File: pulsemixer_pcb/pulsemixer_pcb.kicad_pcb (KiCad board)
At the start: 2 copper layers, 93 parts, among them SW101 SW_PG_RIGHT, SW102 SW_PG_LEFT, SW103 SW_STRM_DEV, SW201 Vol_Encoder, SW202 SW_MUTE, SW301 Vol_Encoder, SW302 SW_MUTE, SW401 Vol_Encoder, SW402 SW_MUTE, SW501 Vol_Encoder, SW502 SW_MUTE, U101 SN74LHC08DR, U102 SN74HC21DR, U201 MCP23017_SP, U202 74LVC2G14, U301 MCP23017_SP, U302 74LVC2G14, U401 MCP23017_SP, U402 74LVC2G14, U501 MCP23017_SP, U502 74LVC2G14

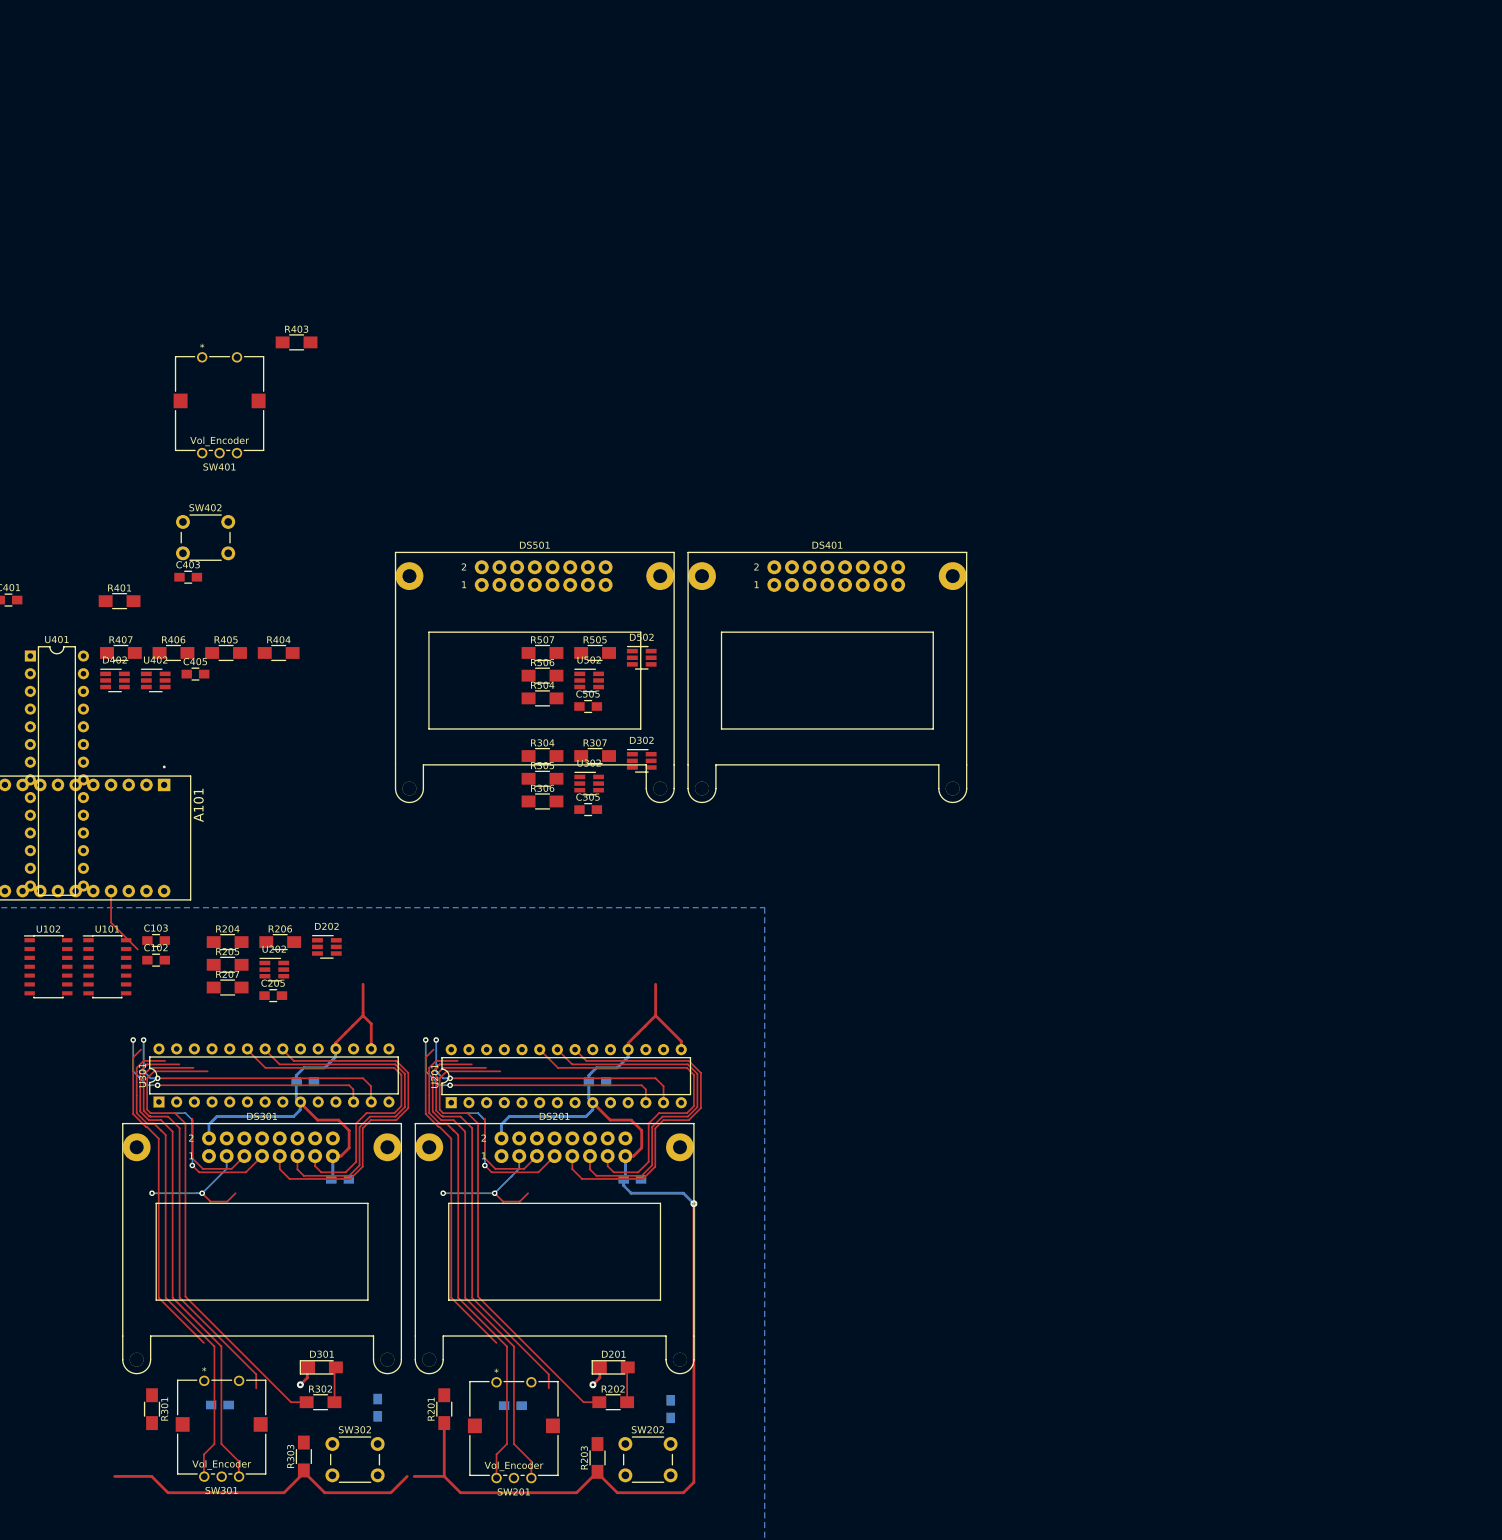
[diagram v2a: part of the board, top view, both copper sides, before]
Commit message: Rearranged LCD pins to allow for interrupts on both GPIO banks.
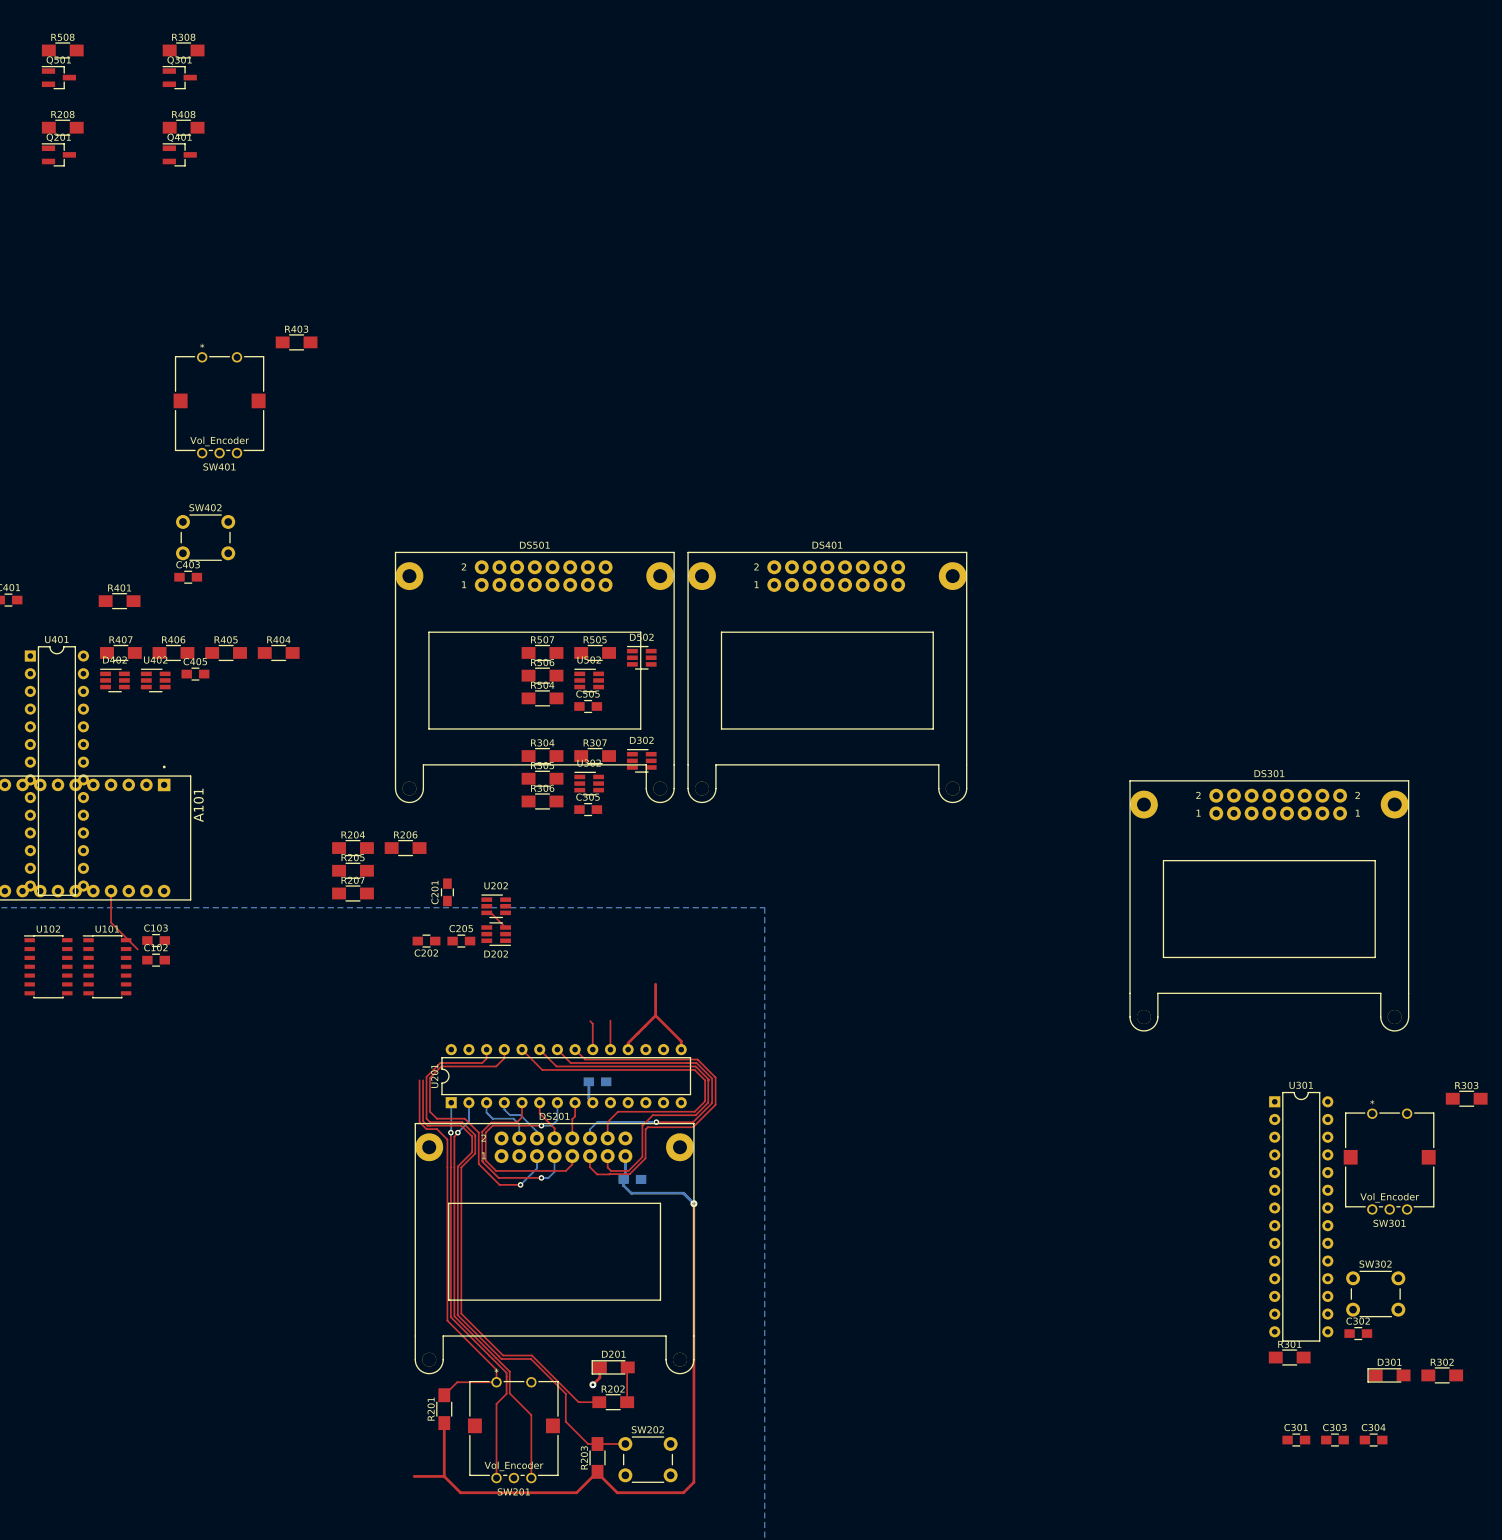
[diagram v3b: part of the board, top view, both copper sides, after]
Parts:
- added Q201: Q_NPN_CBE, TO_SOT_Packages_SMD:SOT-23_Handsoldering, F.Cu at (98.8, -86.1)
- added Q301: Q_NPN_CBE, TO_SOT_Packages_SMD:SOT-23_Handsoldering, F.Cu at (116.2, -97.2)
- added Q401: Q_NPN_CBE, TO_SOT_Packages_SMD:SOT-23_Handsoldering, F.Cu at (116.2, -86.1)
- added Q501: Q_NPN_CBE, TO_SOT_Packages_SMD:SOT-23_Handsoldering, F.Cu at (98.8, -97.2)
- added R208: 1K, Resistors_SMD:R_1206_HandSoldering, F.Cu at (99.4, -90.0)
- added R308: 1K, Resistors_SMD:R_1206_HandSoldering, F.Cu at (116.7, -101.1)
- added R408: 1K, Resistors_SMD:R_1206_HandSoldering, F.Cu at (116.7, -90.0)
- added R508: 1K, Resistors_SMD:R_1206_HandSoldering, F.Cu at (99.4, -101.1)
- C201, C202, C301, C302, C303, C304: moved to F.Cu
- moved R303 174.7 mm to (300.9, 49.4), turned to 0 degrees
- moved SW301 172.0 mm to (289.9, 72.4)
- moved C302 163.8 mm to (285.4, 83.2), turned to 0 degrees
- moved R301 163.5 mm to (275.5, 86.6), turned to 0 degrees
- moved R302 161.1 mm to (297.4, 89.2)
- moved U301 160.2 mm to (273.4, 49.9), turned to 0 degrees
- moved C303 156.5 mm to (282.0, 98.4)
- moved D301 153.3 mm to (289.9, 89.2)
- moved C304 153.0 mm to (287.6, 98.4)
- moved DS301 152.8 mm to (272.6, 3.80)
- moved SW302 148.5 mm to (284.6, 75.2)
- moved C301 132.0 mm to (276.5, 98.4), turned to 0 degrees
- moved C201 80.8 mm to (154.6, 19.8), turned to 90 degrees
- moved C202 67.8 mm to (151.6, 26.8)
- moved U202 33.1 mm to (161.6, 21.8)
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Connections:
- DS201 pad 16: GND -> Net-(DS201-Pad16)
- DS301 pad 16: GND -> Net-(DS301-Pad16)
- DS401 pad 16: GND -> Net-(DS401-Pad16)
- DS501 pad 16: GND -> Net-(DS501-Pad16)
- U201 pad 1: /Channel1/MUTE_SW -> /Channel1/VOL_A
- U201 pad 2: /Channel1/VOL_SW -> /Channel1/VOL_B
- U201 pad 21: /Channel1/LCD_DB2 -> /Channel1/LCD_DB4
- U201 pad 22: /Channel1/LCD_DB4 -> /Channel1/LCD_DB5
- U201 pad 24: /Channel1/LCD_DB5 -> /Channel1/LCD_DB7
- U201 pad 25: /Channel1/LCD_DB7 -> /Channel1/LCD_RW
- U201 pad 27: /Channel1/VOL_B -> /Channel1/MUTE_SW
- U201 pad 28: /Channel1/VOL_A -> /Channel1/VOL_SW
- U201 pad 3: /Channel1/LCD_DB0 -> /Channel1/LCD_RS
- U201 pad 4: /Channel1/LCD_RW -> /Channel1/LCD_E
- U201 pad 5: /Channel1/LCD_RS -> /Channel1/LCD_DB0
- U201 pad 6: /Channel1/LCD_E -> /Channel1/LCD_DB1
- U201 pad 7: /Channel1/LCD_DB1 -> /Channel1/LCD_DB2
- U301 pad 1: /Channel2/MUTE_SW -> /Channel2/VOL_A
- U301 pad 2: /Channel2/VOL_SW -> /Channel2/VOL_B
- U301 pad 21: /Channel2/LCD_DB2 -> /Channel2/LCD_DB4
- U301 pad 22: /Channel2/LCD_DB4 -> /Channel2/LCD_DB5
- U301 pad 24: /Channel2/LCD_DB5 -> /Channel2/LCD_DB7
- U301 pad 25: /Channel2/LCD_DB7 -> /Channel2/LCD_RW
- U301 pad 27: /Channel2/VOL_B -> /Channel2/MUTE_SW
- U301 pad 28: /Channel2/VOL_A -> /Channel2/VOL_SW
- U301 pad 3: /Channel2/LCD_DB0 -> /Channel2/LCD_RS
- U301 pad 4: /Channel2/LCD_RW -> /Channel2/LCD_E
- U301 pad 5: /Channel2/LCD_RS -> /Channel2/LCD_DB0
- U301 pad 6: /Channel2/LCD_E -> /Channel2/LCD_DB1
- U301 pad 7: /Channel2/LCD_DB1 -> /Channel2/LCD_DB2
- U401 pad 1: /Channel3/MUTE_SW -> /Channel3/VOL_A
- U401 pad 2: /Channel3/VOL_SW -> /Channel3/VOL_B
- U401 pad 21: /Channel3/LCD_DB2 -> /Channel3/LCD_DB4
- U401 pad 22: /Channel3/LCD_DB4 -> /Channel3/LCD_DB5
- U401 pad 24: /Channel3/LCD_DB5 -> /Channel3/LCD_DB7
- U401 pad 25: /Channel3/LCD_DB7 -> /Channel3/LCD_RW
- U401 pad 27: /Channel3/VOL_B -> /Channel3/MUTE_SW
- U401 pad 28: /Channel3/VOL_A -> /Channel3/VOL_SW
- U401 pad 3: /Channel3/LCD_DB0 -> /Channel3/LCD_RS
- U401 pad 4: /Channel3/LCD_RW -> /Channel3/LCD_E
- U401 pad 5: /Channel3/LCD_RS -> /Channel3/LCD_DB0
- U401 pad 6: /Channel3/LCD_E -> /Channel3/LCD_DB1
- U401 pad 7: /Channel3/LCD_DB1 -> /Channel3/LCD_DB2
- U501 pad 1: /Channel0/MUTE_SW -> /Channel0/VOL_A
- U501 pad 2: /Channel0/VOL_SW -> /Channel0/VOL_B
- U501 pad 21: /Channel0/LCD_DB2 -> /Channel0/LCD_DB4
- U501 pad 22: /Channel0/LCD_DB4 -> /Channel0/LCD_DB5
- U501 pad 24: /Channel0/LCD_DB5 -> /Channel0/LCD_DB7
- U501 pad 25: /Channel0/LCD_DB7 -> /Channel0/LCD_RW
- U501 pad 27: /Channel0/VOL_B -> /Channel0/MUTE_SW
- U501 pad 28: /Channel0/VOL_A -> /Channel0/VOL_SW
- U501 pad 3: /Channel0/LCD_DB0 -> /Channel0/LCD_RS
- U501 pad 4: /Channel0/LCD_RW -> /Channel0/LCD_E
- U501 pad 5: /Channel0/LCD_RS -> /Channel0/LCD_DB0
- U501 pad 6: /Channel0/LCD_E -> /Channel0/LCD_DB1
- U501 pad 7: /Channel0/LCD_DB1 -> /Channel0/LCD_DB2
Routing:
- net +5V: track 288.2 -> 138.7 mm
- net /SDA: track 80.8 -> 0.00 mm, vias 4 -> 0
- net /SCK: track 78.2 -> 0.00 mm, vias 4 -> 0
- net Net-(D202-Pad1): track 0.00 -> 74.5 mm
- net /Channel2/VOL_B: track 71.3 -> 0.00 mm
- net /Channel2/VOL_A: track 69.2 -> 0.00 mm
- net /Channel2/MUTE_LED: track 68.5 -> 0.00 mm
- net /Channel2/MUTE_SW: track 60.8 -> 0.00 mm
- net /Channel1/MUTE_SW: track 60.8 -> 0.00 mm
- net Net-(D202-Pad4): track 0.00 -> 57.1 mm
- net /Channel2/LCD_DB2: track 52.8 -> 0.00 mm
- net /Channel2/LCD_DB4: track 51.3 -> 0.00 mm
- net /Channel2/LCD_DB6: track 49.5 -> 0.00 mm
- net /Channel1/LCD_DB7: track 0.45 -> 48.7 mm
- net /Channel1/LCD_DB5: track 0.45 -> 47.9 mm, vias 0 -> 1
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
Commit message: Finished full PCB layout.
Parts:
- added C104: 0.1µ, Capacitors_SMD:C_0805_HandSoldering, F.Cu at (95.5, 43.4)
- added C105: 0.1µ, Capacitors_SMD:C_0805_HandSoldering, F.Cu at (83.8, 43.4)
- added C106: 0.1µ, Capacitors_SMD:C_0805_HandSoldering, F.Cu at (112.5, 43.4)
- added C107: 0.1µ, Capacitors_SMD:C_0805_HandSoldering, B.Cu at (129.5, 41.1)
- added D101: D_Schottky, Diodes_SMD:D_1206, F.Cu at (103.1, 43.7)
- added D102: D_Schottky, Diodes_SMD:D_1206, F.Cu at (91.4, 43.7)
- added D103: D_Schottky, Diodes_SMD:D_1206, F.Cu at (119.9, 43.7)
- added D104: D_Schottky, Diodes_SMD:D_1206, F.Cu at (74.7, 49.3)
- added D105: LED, LEDs:LED_1206_HandSoldering, F.Cu at (110.7, 53.1)
- added R107: 1K, Resistors_SMD:R_1206, F.Cu at (87.9, 43.7)
- added R108: 10K, Resistors_SMD:R_1206, F.Cu at (104.1, 39.4)
- added R109: 10K, Resistors_SMD:R_1206, F.Cu at (90.4, 39.4)
- added R110: 250, Resistors_SMD:R_1206, F.Cu at (78.2, 49.3)
- added R111: 150, Resistors_SMD:R_1206, F.Cu at (109.5, 37.6)
- added U103: 74LVC3G17, Housings_SSOP:SSOP-8_2.95x2.8mm_Pitch0.65mm, F.Cu at (127.6, 45.3)
- C101: value 10µ -> 100µ; footprint Capacitors_THT:CP_Radial_D5.0mm_P2.00mm -> Capacitors_THT:CP_Radial_D8.0mm_P3.50mm
- C102, C103, C201, C202, C301, C302, C303, C304, C401, C402, C403, C404, C501, C502, C503, C504: moved to B.Cu
- D201, D301, D401, D501: value LED -> LED_RED
- D202, D302, D402, D502: footprint TO_SOT_Packages_SMD:SOT-23-6_Handsoldering -> pulsemixer_pcb:Diode_Dual_SOT-23-6
- Q201, Q301, Q401, Q501: value Q_NPN_CBE -> Q_NPN_BEC; footprint TO_SOT_Packages_SMD:SOT-23_Handsoldering -> TO_SOT_Packages_SMD:SOT-23; moved to B.Cu
- R101, R102, R104, R106, R201, R202, R203, R204, R205, R206, R207, R301, R302, R303, R304, R305, R306, R307, R401, R402, R403, R404, R405, R406, R407, R501, R502, R503, R504, R505, R506, R507: footprint Resistors_SMD:R_1206_HandSoldering -> Resistors_SMD:R_1206
- R103, R105: value 10K -> 1K; footprint Resistors_SMD:R_1206_HandSoldering -> Resistors_SMD:R_1206
- R208, R308, R408, R508: footprint Resistors_SMD:R_1206_HandSoldering -> Resistors_SMD:R_1206; moved to B.Cu
- SW101: value SW_PG_RIGHT -> SW_PUSH_SPST
- SW102: value SW_PG_LEFT -> SW_PUSH_SPST
- SW103: value SW_STRM_DEV -> SW_PUSH_SPST
- SW202, SW302, SW402, SW502: value SW_MUTE -> SW_PUSH_SPST
- U202, U302, U402, U502: value 74LVC2G14 -> 74LVC2G17; footprint TO_SOT_Packages_SMD:SOT-23-6_Handsoldering -> TO_SOT_Packages_SMD:SOT-23-6
- moved R503 274.4 mm to (227.8, 122.8), turned to 270 degrees
- moved C501 257.7 mm to (224.8, 123.3), turned to 90 degrees
- moved R501 254.5 mm to (195.4, 124.0), turned to 90 degrees
- moved D501 251.5 mm to (216.3, 131.3), turned to 90 degrees
- moved C502 251.4 mm to (213.5, 120.5), turned to 90 degrees
- moved SW502 246.0 mm to (221.4, 129.0)
- moved C504 243.9 mm to (222.4, 81.5)
- moved R502 238.3 mm to (216.3, 123.8), turned to 270 degrees
- moved R101 232.7 mm to (200.8, 58.7), turned to 180 degrees
- moved SW501 231.3 mm to (205.3, 127.0)
- moved R508 228.2 mm to (223.3, 90.5), turned to 180 degrees
- moved Q501 223.2 mm to (230.7, 82.9)
- moved U501 214.1 mm to (196.4, 70.5), turned to 90 degrees
- moved C503 201.7 mm to (217.4, 67.5)
- moved R308 193.1 mm to (140.6, 90.5), turned to 180 degrees
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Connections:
- net Net-(C201-Pad2) renamed /Channel0/MUTE_SW_RC
- net Net-(C202-Pad2) renamed /Channel0/VOL_SW_RC
- net Net-(C301-Pad2) renamed /Channel1/MUTE_SW_RC
- net Net-(C302-Pad2) renamed /Channel1/VOL_SW_RC
- net Net-(C401-Pad2) renamed /Channel2/MUTE_SW_RC
- net Net-(C402-Pad2) renamed /Channel2/VOL_SW_RC
- net Net-(C501-Pad2) renamed /Channel3/MUTE_SW_RC
- net Net-(C502-Pad2) renamed /Channel3/VOL_SW_RC
- net Net-(D201-Pad2) renamed /Channel0/MUTE_LED_TO_D
- net Net-(D202-Pad1) renamed /Channel0/SW_MUTE_OUT
- net Net-(D202-Pad4) renamed /Channel0/SW_VOL_OUT
- net Net-(D301-Pad2) renamed /Channel1/MUTE_LED_TO_D
- net Net-(D302-Pad1) renamed /Channel1/SW_MUTE_OUT
- net Net-(D302-Pad4) renamed /Channel1/SW_VOL_OUT
- net Net-(D401-Pad2) renamed /Channel2/MUTE_LED_TO_D
- net Net-(D402-Pad1) renamed /Channel2/SW_MUTE_OUT
- net Net-(D402-Pad4) renamed /Channel2/SW_VOL_OUT
- net Net-(D501-Pad2) renamed /Channel3/MUTE_LED_TO_D
- net Net-(D502-Pad1) renamed /Channel3/SW_MUTE_OUT
- net Net-(D502-Pad4) renamed /Channel3/SW_VOL_OUT
- A101 pad 12: /STRM_DEV -> /PAGE_BTN
- A101 pad 13: /PAGE_LEFT_BTN -> /IO_BTN
- A101 pad 14: /PAGE_RIGHT_BTN -> /STRM_DEV
- A101 pad 15: (no net) -> Net-(A101-Pad15)
- C101 pad 1: +5V -> Net-(C101-Pad1)
- DS201 pad 10: /Channel1/LCD_DB3 -> (no net)
- DS201 pad 11: /Channel1/LCD_DB4 -> /Channel0/LCD_DB4
- DS201 pad 12: /Channel1/LCD_DB5 -> /Channel0/LCD_DB5
- DS201 pad 13: /Channel1/LCD_DB6 -> /Channel0/LCD_DB6
- DS201 pad 14: /Channel1/LCD_DB7 -> /Channel0/LCD_DB7
- DS201 pad 16: Net-(DS201-Pad16) -> /Channel0/LCD_LED-
- DS201 pad 4: /Channel1/LCD_RS -> /Channel0/LCD_RS
- DS201 pad 5: /Channel1/LCD_RW -> /Channel0/LCD_RW
- DS201 pad 6: /Channel1/LCD_E -> /Channel0/LCD_E
- DS201 pad 7: /Channel1/LCD_DB0 -> (no net)
- DS201 pad 8: /Channel1/LCD_DB1 -> (no net)
- DS201 pad 9: /Channel1/LCD_DB2 -> (no net)
- DS301 pad 10: /Channel2/LCD_DB3 -> (no net)
- DS301 pad 11: /Channel2/LCD_DB4 -> /Channel1/LCD_DB4
- DS301 pad 12: /Channel2/LCD_DB5 -> /Channel1/LCD_DB5
- DS301 pad 13: /Channel2/LCD_DB6 -> /Channel1/LCD_DB6
- DS301 pad 14: /Channel2/LCD_DB7 -> /Channel1/LCD_DB7
- DS301 pad 16: Net-(DS301-Pad16) -> /Channel1/LCD_LED-
- DS301 pad 4: /Channel2/LCD_RS -> /Channel1/LCD_RS
- DS301 pad 5: /Channel2/LCD_RW -> /Channel1/LCD_RW
- DS301 pad 6: /Channel2/LCD_E -> /Channel1/LCD_E
- DS301 pad 7: /Channel2/LCD_DB0 -> (no net)
- DS301 pad 8: /Channel2/LCD_DB1 -> (no net)
- DS301 pad 9: /Channel2/LCD_DB2 -> (no net)
- DS401 pad 10: /Channel3/LCD_DB3 -> (no net)
- DS401 pad 11: /Channel3/LCD_DB4 -> /Channel2/LCD_DB4
- DS401 pad 12: /Channel3/LCD_DB5 -> /Channel2/LCD_DB5
- DS401 pad 13: /Channel3/LCD_DB6 -> /Channel2/LCD_DB6
- DS401 pad 14: /Channel3/LCD_DB7 -> /Channel2/LCD_DB7
- DS401 pad 16: Net-(DS401-Pad16) -> /Channel2/LCD_LED-
- DS401 pad 4: /Channel3/LCD_RS -> /Channel2/LCD_RS
- DS401 pad 5: /Channel3/LCD_RW -> /Channel2/LCD_RW
- DS401 pad 6: /Channel3/LCD_E -> /Channel2/LCD_E
- DS401 pad 7: /Channel3/LCD_DB0 -> (no net)
- DS401 pad 8: /Channel3/LCD_DB1 -> (no net)
- DS401 pad 9: /Channel3/LCD_DB2 -> (no net)
- DS501 pad 10: /Channel0/LCD_DB3 -> (no net)
- DS501 pad 11: /Channel0/LCD_DB4 -> /Channel3/LCD_DB4
- DS501 pad 12: /Channel0/LCD_DB5 -> /Channel3/LCD_DB5
- DS501 pad 13: /Channel0/LCD_DB6 -> /Channel3/LCD_DB6
- DS501 pad 14: /Channel0/LCD_DB7 -> /Channel3/LCD_DB7
- DS501 pad 16: Net-(DS501-Pad16) -> /Channel3/LCD_LED-
- DS501 pad 4: /Channel0/LCD_RS -> /Channel3/LCD_RS
- DS501 pad 5: /Channel0/LCD_RW -> /Channel3/LCD_RW
- DS501 pad 6: /Channel0/LCD_E -> /Channel3/LCD_E
- DS501 pad 7: /Channel0/LCD_DB0 -> (no net)
- DS501 pad 8: /Channel0/LCD_DB1 -> (no net)
- DS501 pad 9: /Channel0/LCD_DB2 -> (no net)
- Q201 pad 1: Net-(DS201-Pad16) -> /Channel0/LCD_LED_B
- Q201 pad 2: Net-(Q201-Pad2) -> /Channel0/LCD_LED-
- Q301 pad 1: Net-(DS301-Pad16) -> /Channel1/LCD_LED_B
- Q301 pad 2: Net-(Q301-Pad2) -> /Channel1/LCD_LED-
- Q401 pad 1: Net-(DS401-Pad16) -> /Channel2/LCD_LED_B
- Q401 pad 2: Net-(Q401-Pad2) -> /Channel2/LCD_LED-
- Q501 pad 1: Net-(DS501-Pad16) -> /Channel3/LCD_LED_B
- Q501 pad 2: Net-(Q501-Pad2) -> /Channel3/LCD_LED-
- R103 pad 1: +5V -> Net-(D101-Pad2)
- R103 pad 2: /PAGE_RIGHT_BTN -> Net-(C104-Pad1)
- R104 pad 1: +5V -> Net-(D103-Pad2)
- R104 pad 2: /PAGE_LEFT_BTN -> +5V
- R105 pad 1: +5V -> Net-(D103-Pad2)
- R105 pad 2: /STRM_DEV -> Net-(C106-Pad1)
- R202 pad 1: /Channel1/MUTE_LED -> /Channel0/MUTE_LED
- R204 pad 2: /Channel1/VOL_B -> /Channel0/VOL_B
- R205 pad 2: /Channel1/VOL_A -> /Channel0/VOL_A
- R208 pad 1: Net-(Q201-Pad2) -> /Channel0/LCD_LED_B
- R208 pad 2: (no net) -> /Channel0/LCD_LED
- R302 pad 1: /Channel2/MUTE_LED -> /Channel1/MUTE_LED
- R304 pad 2: /Channel2/VOL_B -> /Channel1/VOL_B
- R305 pad 2: /Channel2/VOL_A -> /Channel1/VOL_A
- R308 pad 1: Net-(Q301-Pad2) -> /Channel1/LCD_LED_B
- R308 pad 2: (no net) -> /Channel1/LCD_LED
- R402 pad 1: /Channel3/MUTE_LED -> /Channel2/MUTE_LED
- R404 pad 2: /Channel3/VOL_B -> /Channel2/VOL_B
- R405 pad 2: /Channel3/VOL_A -> /Channel2/VOL_A
- R408 pad 1: Net-(Q401-Pad2) -> /Channel2/LCD_LED_B
- R408 pad 2: (no net) -> /Channel2/LCD_LED
- R502 pad 1: /Channel0/MUTE_LED -> /Channel3/MUTE_LED
- R504 pad 2: /Channel0/VOL_B -> /Channel3/VOL_B
- R505 pad 2: /Channel0/VOL_A -> /Channel3/VOL_A
- R508 pad 1: Net-(Q501-Pad2) -> /Channel3/LCD_LED_B
- R508 pad 2: (no net) -> /Channel3/LCD_LED
- SW101 pad 1: /PAGE_RIGHT_BTN -> Net-(D101-Pad2)
- SW102 pad 1: /PAGE_LEFT_BTN -> Net-(D102-Pad2)
- SW103 pad 1: /STRM_DEV -> Net-(D103-Pad2)
- SW201 pad A: /Channel1/VOL_A -> /Channel0/VOL_A
- SW201 pad B: /Channel1/VOL_B -> /Channel0/VOL_B
- SW301 pad A: /Channel2/VOL_A -> /Channel1/VOL_A
- SW301 pad B: /Channel2/VOL_B -> /Channel1/VOL_B
- SW401 pad A: /Channel3/VOL_A -> /Channel2/VOL_A
- SW401 pad B: /Channel3/VOL_B -> /Channel2/VOL_B
- SW501 pad A: /Channel0/VOL_A -> /Channel3/VOL_A
- SW501 pad B: /Channel0/VOL_B -> /Channel3/VOL_B
- U101 pad 1: /INTBTN_CH0 -> /INTVOL_CH0
- U101 pad 10: /INTVOL_CH2 -> /INTBTN_CH2
- U101 pad 2: /INTVOL_CH0 -> /INTBTN_CH0
- U101 pad 4: /INTBTN_CH1 -> /INTVOL_CH1
- U101 pad 5: /INTVOL_CH1 -> /INTBTN_CH1
- U101 pad 9: /INTBTN_CH2 -> /INTVOL_CH2
- U201 pad 1: /Channel1/VOL_A -> /Channel0/VOL_A
- U201 pad 19: /INTBTN_CH1 -> /INTBTN_CH0
- U201 pad 2: /Channel1/VOL_B -> /Channel0/VOL_B
- U201 pad 20: /INTVOL_CH1 -> /INTVOL_CH0
- U201 pad 21: /Channel1/LCD_DB4 -> /Channel0/LCD_DB4
- U201 pad 22: /Channel1/LCD_DB5 -> /Channel0/LCD_DB5
- U201 pad 23: /Channel1/LCD_DB6 -> /Channel0/LCD_DB6
- U201 pad 24: /Channel1/LCD_DB7 -> /Channel0/LCD_DB7
- U201 pad 25: /Channel1/LCD_RW -> (no net)
- U201 pad 26: /Channel1/MUTE_LED -> /Channel0/MUTE_SW
- U201 pad 27: /Channel1/MUTE_SW -> /Channel0/VOL_SW
- U201 pad 28: /Channel1/VOL_SW -> /Channel0/MUTE_LED
- U201 pad 3: /Channel1/LCD_RS -> /Channel0/LCD_RS
- U201 pad 4: /Channel1/LCD_E -> /Channel0/LCD_E
- U201 pad 5: /Channel1/LCD_DB0 -> /Channel0/LCD_LED
- U201 pad 6: /Channel1/LCD_DB1 -> /Channel0/LCD_RW
- U201 pad 7: /Channel1/LCD_DB2 -> (no net)
- U201 pad 8: /Channel1/LCD_DB3 -> (no net)
- U202 pad 4: /Channel1/VOL_SW -> /Channel0/VOL_SW
- U202 pad 6: /Channel1/MUTE_SW -> /Channel0/MUTE_SW
- U301 pad 1: /Channel2/VOL_A -> /Channel1/VOL_A
- U301 pad 19: /INTBTN_CH2 -> /INTBTN_CH1
- U301 pad 2: /Channel2/VOL_B -> /Channel1/VOL_B
- U301 pad 20: /INTVOL_CH2 -> /INTVOL_CH1
- U301 pad 21: /Channel2/LCD_DB4 -> /Channel1/LCD_DB4
- U301 pad 22: /Channel2/LCD_DB5 -> /Channel1/LCD_DB5
- U301 pad 23: /Channel2/LCD_DB6 -> /Channel1/LCD_DB6
- U301 pad 24: /Channel2/LCD_DB7 -> /Channel1/LCD_DB7
- U301 pad 25: /Channel2/LCD_RW -> (no net)
- U301 pad 26: /Channel2/MUTE_LED -> /Channel1/MUTE_SW
- U301 pad 27: /Channel2/MUTE_SW -> /Channel1/VOL_SW
- U301 pad 28: /Channel2/VOL_SW -> /Channel1/MUTE_LED
- U301 pad 3: /Channel2/LCD_RS -> /Channel1/LCD_RS
- U301 pad 4: /Channel2/LCD_E -> /Channel1/LCD_E
- U301 pad 5: /Channel2/LCD_DB0 -> /Channel1/LCD_LED
- U301 pad 6: /Channel2/LCD_DB1 -> /Channel1/LCD_RW
- U301 pad 7: /Channel2/LCD_DB2 -> (no net)
- U301 pad 8: /Channel2/LCD_DB3 -> (no net)
- U302 pad 4: /Channel2/VOL_SW -> /Channel1/VOL_SW
- U302 pad 6: /Channel2/MUTE_SW -> /Channel1/MUTE_SW
- U401 pad 1: /Channel3/VOL_A -> /Channel2/VOL_A
- U401 pad 19: /INTBTN_CH3 -> /INTBTN_CH2
- U401 pad 2: /Channel3/VOL_B -> /Channel2/VOL_B
- U401 pad 20: /INTVOL_CH3 -> /INTVOL_CH2
- U401 pad 21: /Channel3/LCD_DB4 -> /Channel2/LCD_DB4
- U401 pad 22: /Channel3/LCD_DB5 -> /Channel2/LCD_DB5
- U401 pad 23: /Channel3/LCD_DB6 -> /Channel2/LCD_DB6
- U401 pad 24: /Channel3/LCD_DB7 -> /Channel2/LCD_DB7
- U401 pad 25: /Channel3/LCD_RW -> (no net)
- U401 pad 26: /Channel3/MUTE_LED -> /Channel2/MUTE_SW
- U401 pad 27: /Channel3/MUTE_SW -> /Channel2/VOL_SW
- U401 pad 28: /Channel3/VOL_SW -> /Channel2/MUTE_LED
- U401 pad 3: /Channel3/LCD_RS -> /Channel2/LCD_RS
- U401 pad 4: /Channel3/LCD_E -> /Channel2/LCD_E
- U401 pad 5: /Channel3/LCD_DB0 -> /Channel2/LCD_LED
- U401 pad 6: /Channel3/LCD_DB1 -> /Channel2/LCD_RW
- U401 pad 7: /Channel3/LCD_DB2 -> (no net)
- U401 pad 8: /Channel3/LCD_DB3 -> (no net)
- U402 pad 4: /Channel3/VOL_SW -> /Channel2/VOL_SW
- U402 pad 6: /Channel3/MUTE_SW -> /Channel2/MUTE_SW
- U501 pad 1: /Channel0/VOL_A -> /Channel3/VOL_A
- U501 pad 19: /INTBTN_CH0 -> /INTBTN_CH3
- U501 pad 2: /Channel0/VOL_B -> /Channel3/VOL_B
- U501 pad 20: /INTVOL_CH0 -> /INTVOL_CH3
- U501 pad 21: /Channel0/LCD_DB4 -> /Channel3/LCD_DB4
- U501 pad 22: /Channel0/LCD_DB5 -> /Channel3/LCD_DB5
- U501 pad 23: /Channel0/LCD_DB6 -> /Channel3/LCD_DB6
- U501 pad 24: /Channel0/LCD_DB7 -> /Channel3/LCD_DB7
- U501 pad 25: /Channel0/LCD_RW -> (no net)
- U501 pad 26: /Channel0/MUTE_LED -> /Channel3/MUTE_SW
- U501 pad 27: /Channel0/MUTE_SW -> /Channel3/VOL_SW
- U501 pad 28: /Channel0/VOL_SW -> /Channel3/MUTE_LED
- U501 pad 3: /Channel0/LCD_RS -> /Channel3/LCD_RS
- U501 pad 4: /Channel0/LCD_E -> /Channel3/LCD_E
- U501 pad 5: /Channel0/LCD_DB0 -> /Channel3/LCD_LED
- U501 pad 6: /Channel0/LCD_DB1 -> /Channel3/LCD_RW
- U501 pad 7: /Channel0/LCD_DB2 -> (no net)
- U501 pad 8: /Channel0/LCD_DB3 -> (no net)
- U502 pad 4: /Channel0/VOL_SW -> /Channel3/VOL_SW
- U502 pad 6: /Channel0/MUTE_SW -> /Channel3/MUTE_SW
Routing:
- net /SDA: track 0.00 -> 330.4 mm, vias 0 -> 10
- net /SCK: track 0.00 -> 323.0 mm, vias 0 -> 10
- net /LCD_V0: track 0.00 -> 275.2 mm, vias 0 -> 5
- net Net-(A101-Pad15): track 0.00 -> 131.6 mm
- net /STRM_DEV: track 0.00 -> 113.0 mm
- net /PAGE_BTN: track 0.00 -> 112.9 mm
- net /INTBTN_CH3: track 0.00 -> 110.7 mm, vias 0 -> 4
- net /IO_BTN: track 0.00 -> 107.9 mm
- net /STRM_DEV_LED: track 0.00 -> 99.0 mm
- net /INTCH1: track 0.00 -> 92.3 mm
- net /INTCH0: track 0.00 -> 91.9 mm
- net /INTCH2: track 0.00 -> 90.3 mm
- net /INTBTN_CH0: track 0.00 -> 88.8 mm, vias 0 -> 3
- net /INTVOL_CH3: track 0.00 -> 87.1 mm, vias 0 -> 4
- net /INTCH3: track 0.00 -> 82.6 mm
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- added copper zone on F.Cu, net +5V
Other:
- board outline added: 177.9 x 112 mm
- board text added: "Channel 0"
- board text added: "Channel 1"
- board text added: "Channel 2"
- board text added: "Channel 3"
- board text added: "Contrast"
- board text added: "Input / Output"
- board text added: "Mute"
- board text added: "Page"
- board text added: "Stream / Device"
- board text added: "Volume"
